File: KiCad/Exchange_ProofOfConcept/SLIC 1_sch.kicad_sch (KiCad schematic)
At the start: 9 parts

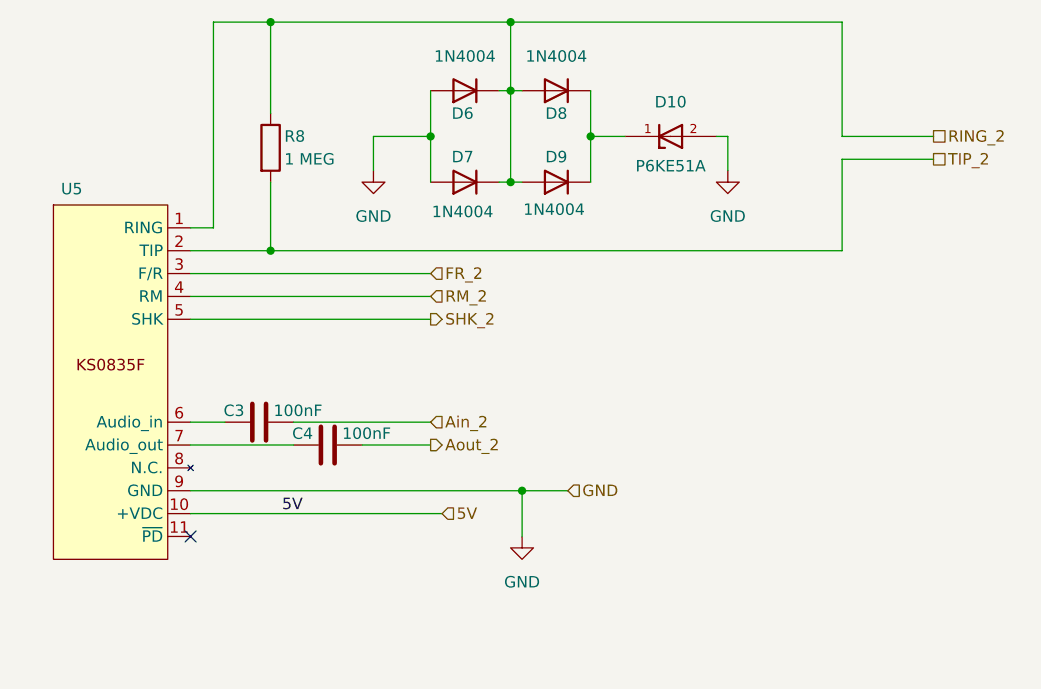
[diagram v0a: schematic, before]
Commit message: deleted:    KiCad/Exchange_ProofOfConcept/Exchange_ProofOfConcept-backups/Exchange_ProofOfConcept-2024-08-28_233227.zip 	deleted:    KiCad/Exchange_ProofOfConcept/Exchange_ProofOfConcept-backups/Exchange_ProofOfConcept-2024-08-28_234504.zip 	deleted:    KiCad/Exchange_ProofOfConcept/Exchange_ProofOfConcept-backups/Exchange_ProofOfConcept-2024-09-04_201626.zip 	deleted:    KiCad/Exchange_ProofOfConcept/Exchange_ProofOfConcept-backups/Exchange_ProofOfConcept-2024-09-04_202659.zip 	deleted:    KiCad/Exchange_ProofOfConcept/Exchange_ProofOfConcept-backups/Exchange_ProofOfConcept-2024-09-04_203703.zip 	deleted:    KiCad/Exchange_ProofOfConcept/Exchange_ProofOfConcept-backups/Exchange_ProofOfConcept-2024-09-04_204710.zip 	deleted:    KiCad/Exchange_ProofOfConcept/Exchange_ProofOfConcept-backups/Exchange_ProofOfConcept-2024-09-04_205754.zip 	deleted:    KiCad/Exchange_ProofOfConcept/Exchange_ProofOfConcept-backups/Exchange_ProofOfConcept-2024-09-05_153643.zip 	deleted:    KiCad/Exchange_ProofOfConcept/Exchange_ProofOfConcept-backups/Exchange_ProofOfConcept-2024-09-05_161017.zip 	deleted:    KiCad/Exchange_ProofOfConcept/Exchange_ProofOfConcept-backups/Exchange_ProofOfConcept-2024-09-05_162441.zip 	deleted:    KiCad/Exchange_ProofOfConcept/Exchange_ProofOfConcept-backups/Exchange_ProofOfConcept-2024-09-05_163641.zip 	deleted:    KiCad/Exchange_ProofOfConcept/Exchange_ProofOfConcept-backups/Exchange_ProofOfConcept-2024-09-06_180233.zip 	deleted:    KiCad/Exchange_ProofOfConcept/Exchange_ProofOfConcept-backups/Exchange_ProofOfConcept-2024-09-06_180943.zip 	deleted:    KiCad/Exchange_ProofOfConcept/Exchange_ProofOfConcept-backups/Exchange_ProofOfConcept-2024-09-06_182256.zip 	deleted:    KiCad/Exchange_ProofOfConcept/Exchange_ProofOfConcept-backups/Exchange_ProofOfConcept-2024-09-06_185314.zip 	deleted:    KiCad/Exchange_ProofOfConcept/Exchange_ProofOfConcept-backups/Exchange_ProofOfConcept-2024-09-06_191143.zip 	deleted:    KiCad/Exchange_ProofOfConcept/Exchange_ProofOfConcep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
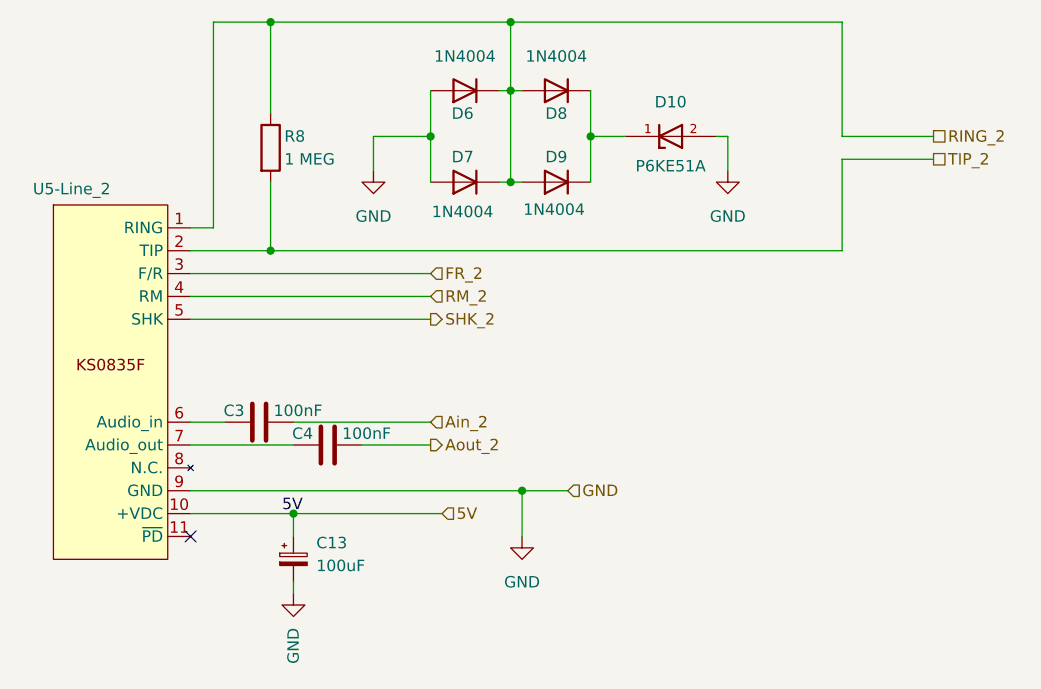
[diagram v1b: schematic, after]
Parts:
- added C13: 100uF, Capacitor_THT:CP_Radial_D5.0mm_P2.00mm, symbol Device:C_Polarized_Small
- renumbered U5 to U5-Line_2
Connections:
- net 5V: now also C13.1
- net GND: now also C13.2
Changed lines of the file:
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@@
+	)
+	(junction
+		(at 62.23 87.63)
+		(diameter 0)
+		(color 0 0 0 0)
 	)
 	(junction
@@
 	(wire
 		(pts
-			(xy 50.8 87.63) (xy 78.74 87.63)
+			(xy 50.8 87.63) (xy 62.23 87.63)
 		)
 		(stroke
@@
 	(wire
 		(pts
+			(xy 62.23 95.25) (xy 62.23 96.52)
+		)
+		(stroke
+			(width 0)
+			(type default)
+		)
+	)
+	(wire
+		(pts
+			(xy 62.23 90.17) (xy 62.23 87.63)
+		)
+		(stroke
+			(width 0)
+			(type default)
+		)
+	)
+	(wire
+		(pts
 			(xy 50.8 66.04) (xy 77.47 66.04)
 		)
@@
 		(pts
 			(xy 86.36 40.64) (xy 86.36 50.8)
+		)
+		(stroke
+			(width 0)
+			(type default)
+		)
+	)
+	(wire
+		(pts
+			(xy 62.23 87.63) (xy 78.74 87.63)
 		)
 		(stroke
@@
 		(on_board yes)
 		(dnp no)
-		(property "Reference" "U5"
+		(property "Reference" "U5-Line_2"
 			(at 37.592 51.562 0)
 			(effects
@@
 			(project "Exchange_ProofOfConcept"
 				(path "/a3aa82f3-37b8-406c-999a-d11513c8e1fa/46552190-bdda-4b98-9908-37a16db58ff7"
-					(reference "U5")
+					(reference "U5-Line_2")
+					(unit 1)
+				)
+			)
+		)
+	)
+	(symbol
+		(lib_id "Device:C_Polarized_Small")
+		(at 62.23 92.71 0)
+		(unit 1)
+		(exclude_from_sim no)
+		(in_bom yes)
+		(on_board yes)
+		(dnp no)
+		(fields_autoplaced yes)
+		(property "Reference" "C13"
+			(at 64.77 90.8938 0)
+			(effects
+				(font
+					(size 1.27 1.27)
+				)
+				(justify left)
+			)
+		)
+		(property "Value" "100uF"
+			(at 64.77 93.4338 0)
+			(effects
+				(font
+					(size 1.27 1.27)
+				)
+				(justify left)
+			)
+		)
+		(property "Footprint" "Capacitor_THT:CP_Radial_D5.0mm_P2.00mm"
+			(at 62.23 92.71 0)
+			(effects
+				(font
+					(size 1.27 1.27)
+				)
+				(hide yes)
+			)
+		)
+		(property "Datasheet" "~"
+			(at 62.23 92.71 0)
+			(effects
+				(font
+					(size 1.27 1.27)
+				)
+				(hide yes)
+			)
+		)
+		(property "Description" "Polarized capacitor, small symbol"
+			(at 62.23 92.71 0)
+			(effects
+				(font
+					(size 1.27 1.27)
+				)
+				(hide yes)
+			)
+		)
+		(pin "1"
+		)
+		(pin "2"
+		)
+		(instances
+			(project "Exchange_ProofOfConcept"
+				(path "/a3aa82f3-37b8-406c-999a-d11513c8e1fa/46552190-bdda-4b98-9908-37a16db58ff7"
+					(reference "C13")
 					(unit 1)
 				)
@@
 					(unit 1)
 				)
+			)
+		)
+	)
+	(symbol
+		(lib_id "power:GND")
+		(at 62.23 96.52 0)
+		(unit 1)
+		(exclude_from_sim no)
+		(in_bom yes)
+		(on_board yes)
+		(dnp no)
+		(fields_autoplaced yes)
+		(property "Reference" "#PWR027"
+			(at 62.23 102.87 0)
+			(effects
+				(font
+					(size 1.27 1.27)
+				)
+				(hide yes)
+			)
+		)
+		(property "Value" "GND"
+			(at 62.2301 100.33 90)
+			(effects
+				(font
+					(size 1.27 1.27)
+				)
+				(justify right)
+			)
+		)
+		(property "Footprint" ""
+			(at 62.23 96.52 0)
+			(effects
+				(font
+					(size 1.27 1.27)
+				)
+				(hide yes)
+			)
+		)
+		(property "Datasheet" ""
+			(at 62.23 96.52 0)
+			(effects
+				(font
+					(size 1.27 1.27)
+				)
+				(hide yes)
+			)
+		)
+		(property "Description" "Power symbol creates a global label with name \"GND\" , ground"
+			(at 62.23 96.52 0)
+			(effects
+				(font
+					(size 1.27 1.27)
+				)
+				(hide yes)
+			)
+		)
+		(pin "1"
+		)
+		(instances
+			(project "Exchange_ProofOfConcept"
+				(path "/a3aa82f3-37b8-406c-999a-d11513c8e1fa/46552190-bdda-4b98-9908-37a16db58ff7"
+					(reference "#PWR027")
+					(unit 1)
+				)

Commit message: new file:   KiCad/Exchange_ProofOfConcept/ESP-Unit/ESP-Unit-backups/ESP-Unit-2024-10-22_204833.zip 	new file:   KiCad/Exchange_ProofOfConcept/ESP-Unit/ESP-Unit-backups/ESP-Unit-2024-10-22_205851.zip 	new file:   KiCad/Exchange_ProofOfConcept/ESP-Unit/ESP-Unit-backups/ESP-Unit-2024-10-22_214835.zip 	new file:   KiCad/Exchange_ProofOfConcept/ESP-Unit/ESP-Unit-backups/ESP-Unit-2024-10-31_190638.zip 	new file:   KiCad/Exchange_ProofOfConcept/ESP-Unit/ESP-Unit.kicad_pcb 	new file:   KiCad/Exchange_ProofOfConcept/ESP-Unit/ESP-Unit.kicad_prl 	new file:   KiCad/Exchange_ProofOfConcept/ESP-Unit/ESP-Unit.kicad_pro 	new file:   KiCad/Exchange_ProofOfConcept/ESP-Unit/ESP-Unit.kicad_sch 	new file:   KiCad/Exchange_ProofOfConcept/ESP-Unit/fp-info-cache 	deleted:    KiCad/Exchange_ProofOfConcept/Exchange_ProofOfConcept-backups/Exchange_ProofOfConcept-2024-09-09_193050.zip 	deleted:    KiCad/Exchange_ProofOfConcept/Exchange_ProofOfConcept-backups/Exchange_ProofOfConcept-2024-09-10_220108.zip 	deleted:    KiCad/Exchange_ProofOfConcept/Exchange_ProofOfConcept-backups/Exchange_ProofOfConcept-2024-09-10_232037.zip 	deleted:    KiCad/Exchange_ProofOfConcept/Exchange_ProofOfConcept-backups/Exchange_ProofOfConcept-2024-09-11_034329.zip 	deleted:    KiCad/Exchange_ProofOfConcept/Exchange_ProofOfConcept-backups/Exchange_ProofOfConcept-2024-09-11_195456.zip 	deleted:    KiCad/Exchange_ProofOfConcept/Exchange_ProofOfConcept-backups/Exchange_ProofOfConcept-2024-09-17_174014.zip 	deleted:    KiCad/Exchange_ProofOfConcept/Exchange_ProofOfConcept-backups/Exchange_ProofOfConcept-2024-09-17_181112.zip 	deleted:    KiCad/Exchange_ProofOfConcept/Exchange_ProofOfConcept-backups/Exchange_ProofOfConcept-2024-09-19_202603.zip 	deleted:    KiCad/Exchange_ProofOfConcept/Exchange_ProofOfConcept-backups/Exchange_ProofOfConcept-2024-09-19_204637.zip 	deleted:    KiCad/Exchange_ProofOfConcept/Exchange_ProofOfConcept-backups/Exchange_ProofOfConcept-2024-09-19_205646.zip 	deleted:    KiCad/Exchange_ProofOfConcep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
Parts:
- R8: footprint Resistor_THT:R_Axial_DIN0204_L3.6mm_D1.6mm_P5.08mm_Horizontal -> Resistor_THT:R_Axial_DIN0207_L6.3mm_D2.5mm_P7.62mm_Horizontal
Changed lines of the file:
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@@
 			)
 		)
-		(property "Footprint" "Resistor_THT:R_Axial_DIN0204_L3.6mm_D1.6mm_P5.08mm_Horizontal"
+		(property "Footprint" "Resistor_THT:R_Axial_DIN0207_L6.3mm_D2.5mm_P7.62mm_Horizontal"
 			(at 57.912 46.99 90)
 			(effects

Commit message: deleted:    KiCad/Exchange_ProofOfConcept/Exchange_ProofOfConcept-backups/Exchange_ProofOfConcept-2024-09-22_005800.zip 	deleted:    KiCad/Exchange_ProofOfConcept/Exchange_ProofOfConcept-backups/Exchange_ProofOfConcept-2024-09-22_010415.zip 	deleted:    KiCad/Exchange_ProofOfConcept/Exchange_ProofOfConcept-backups/Exchange_ProofOfConcept-2024-09-22_093037.zip 	deleted:    KiCad/Exchange_ProofOfConcept/Exchange_ProofOfConcept-backups/Exchange_ProofOfConcept-2024-09-22_093847.zip 	deleted:    KiCad/Exchange_ProofOfConcept/Exchange_ProofOfConcept-backups/Exchange_ProofOfConcept-2024-09-22_094927.zip 	deleted:    KiCad/Exchange_ProofOfConcept/Exchange_ProofOfConcept-backups/Exchange_ProofOfConcept-2024-10-02_184119.zip 	deleted:    KiCad/Exchange_ProofOfConcept/Exchange_ProofOfConcept-backups/Exchange_ProofOfConcept-2024-10-06_223658.zip 	new file:   KiCad/Exchange_ProofOfConcept/Exchange_ProofOfConcept-backups/Exchange_ProofOfConcept-2024-11-20_223020.zip 	new file:   KiCad/Exchange_ProofOfConcept/Exchange_ProofOfConcept-backups/Exchange_ProofOfConcept-2024-11-20_223933.zip 	new file:   KiCad/Exchange_ProofOfConcept/Exchange_ProofOfConcept-backups/Exchange_ProofOfConcept-2024-11-20_224852.zip 	new file:   KiCad/Exchange_ProofOfConcept/Exchange_ProofOfConcept-backups/Exchange_ProofOfConcept-2024-11-20_230009.zip 	new file:   KiCad/Exchange_ProofOfConcept/Exchange_ProofOfConcept-backups/Exchange_ProofOfConcept-2024-11-20_231023.zip 	new file:   KiCad/Exchange_ProofOfConcept/Exchange_ProofOfConcept-backups/Exchange_ProofOfConcept-2024-11-20_231736.zip 	modified:   KiCad/Exchange_ProofOfConcept/Exchange_ProofOfConcept.kicad_pcb 	modified:   KiCad/Exchange_ProofOfConcept/Exchange_ProofOfConcept.kicad_prl 	modified:   KiCad/Exchange_ProofOfConcept/Exchange_ProofOfConcept.kicad_pro 	modified:   KiCad/Exchange_ProofOfConcept/Exchange_ProofOfConcept.kicad_sch 	modified:   KiCad/Exchange_ProofOfConcept/SLIC 1.kicad_sch 	modified:   KiCad/Exchange_ProofOfConcept/SLIC 1_sch.kicad_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
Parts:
- R8: footprint Resistor_THT:R_Axial_DIN0207_L6.3mm_D2.5mm_P7.62mm_Horizontal -> Resistor_THT:R_Axial_DIN0207_L6.3mm_D2.5mm_P2.54mm_Vertical
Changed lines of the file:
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@@
 			)
 		)
-		(property "Footprint" "Resistor_THT:R_Axial_DIN0207_L6.3mm_D2.5mm_P7.62mm_Horizontal"
+		(property "Footprint" "Resistor_THT:R_Axial_DIN0207_L6.3mm_D2.5mm_P2.54mm_Vertical"
 			(at 57.912 46.99 90)
 			(effects
